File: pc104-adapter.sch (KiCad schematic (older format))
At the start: 12 parts, among them J1 Conn_01x13_Male, J10 SAMTEC-TSW-126-07-X-D, J2 Conn_01x13_Male, J3 Conn_01x13_Male, J4 Conn_01x13_Male, J5 Conn_01x13_Male, J6 Conn_01x13_Male, J7 Conn_01x13_Male, J8 Conn_01x13_Male, J9 SAMTEC-TSW-126-07-X-D

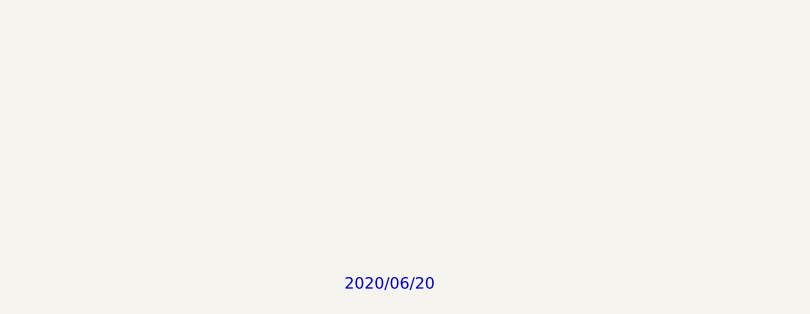
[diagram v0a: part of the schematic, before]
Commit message: schematic: Adding metadata #2
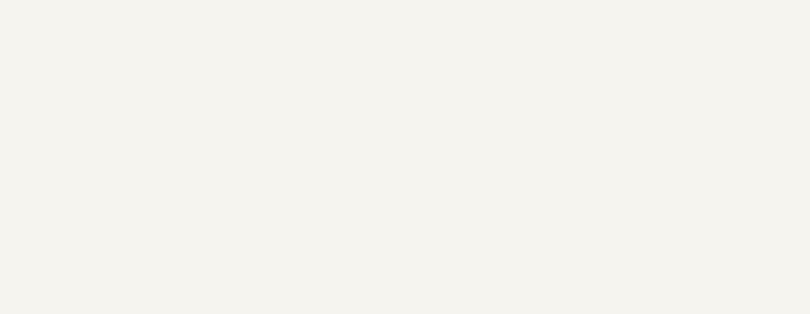
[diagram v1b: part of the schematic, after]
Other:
- note removed: "2020/06/20"
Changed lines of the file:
@@
 encoding utf-8
 Sheet 1 1
-Title ""
-Date ""
-Rev ""
-Comp ""
-Comment1 ""
+Title "PC-104 to PicoBlade Adapter (Bottom)"
+Date "2020-06-21"
+Rev "v1.0"
+Comp "SpaceLab"
+Comment1 "Author: Gabriel Mariano Marcelino"
 Comment2 ""
 Comment3 ""
@@
 Wire Wire Line
 	9850 1500 10050 1500
-Text Notes 8150 7650 0    50   ~ 0
-2020/06/20
 $Comp
 L Connector:Conn_01x13_Male J1
